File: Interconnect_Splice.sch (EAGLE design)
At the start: 4 parts, among them J1 POWER_JACKPTH, J2 POWER_JACKPTH

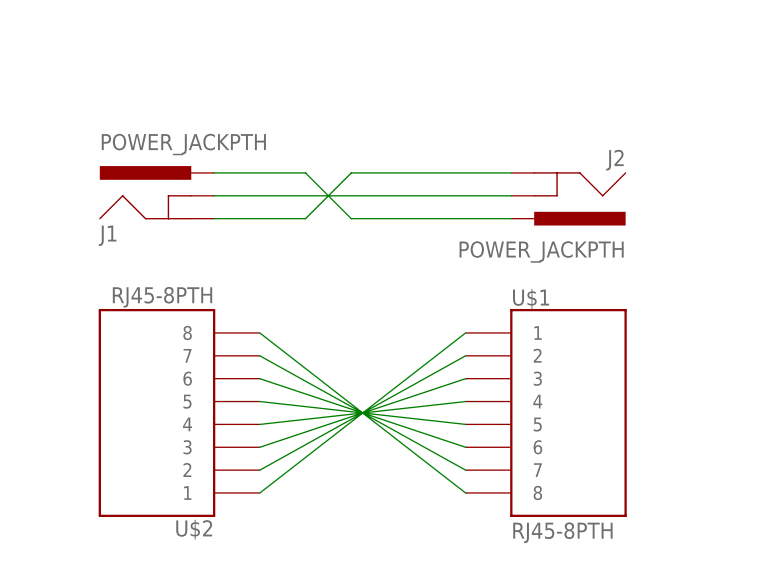
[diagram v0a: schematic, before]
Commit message: fixed bbb cape issue, did something with cable splice
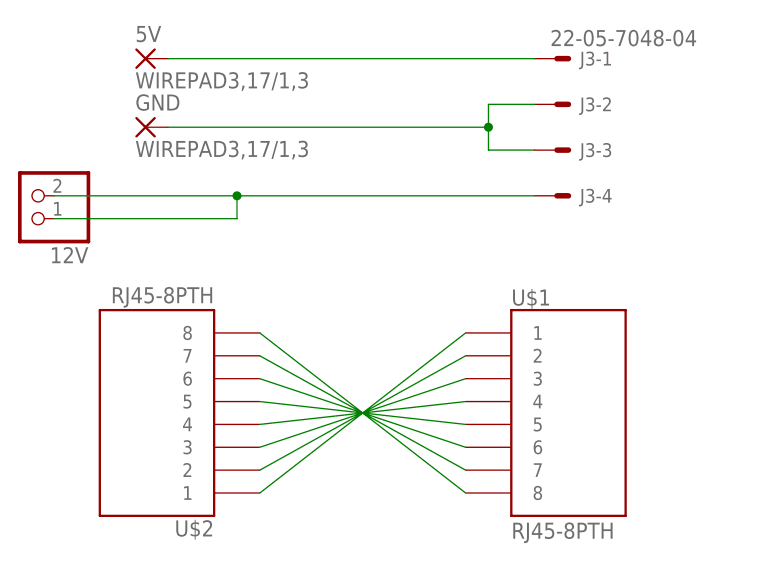
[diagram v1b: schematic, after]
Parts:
- removed J1, J2: POWER_JACKPTH, SparkFun-Connectors:POWER_JACKPTH
- added 12V: (no value), pinhead:PINHD-1X2/90
- added 5V, GND: WIREPAD3,17/1,3, wirepad:WIREPAD3,17/1,3
- added J3: 22-05-7048-04, con-molex:22-05-7048-04
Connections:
- removed net N$1: J1.GND, J2.GND
- new net GND: GND.P, J3-2.S, J3-3.S
- net N$2: now also 5V.P, J3-1.S; no longer J1.GNDBREAK, J2.GNDBREAK
- net N$3: now also 12V.1, 12V.2, J3-4.S; no longer J1.PWR, J2.PWR
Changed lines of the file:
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@@
 <part name="U$1" library="SparkFun-Connectors" deviceset="RJ45-8" device="PTH"/>
 <part name="U$2" library="SparkFun-Connectors" deviceset="RJ45-8" device="PTH"/>
-<part name="J1" library="SparkFun-Connectors" deviceset="POWER_JACK" device="PTH"/>
-<part name="J2" library="SparkFun-Connectors" deviceset="POWER_JACK" device="PTH"/>
+<part name="J3" library="con-molex" deviceset="22-?-04" device="05-7048"/>
+<part name="GND" library="wirepad" deviceset="WIREPAD" device="3,17/1,3" value="WIREPAD3,17/1,3"/>
+<part name="5V" library="wirepad" deviceset="WIREPAD" device="3,17/1,3" value="WIREPAD3,17/1,3"/>
+<part name="12V" library="pinhead" deviceset="PINHD-1X2" device="/90"/>
 </parts>
 <sheets>
@@
 <instance part="U$1" gate="G$1" x="76.2" y="40.64"/>
 <instance part="U$2" gate="G$1" x="27.94" y="43.18" rot="R180"/>
-<instance part="J1" gate="G$1" x="33.02" y="60.96"/>
-<instance part="J2" gate="G$1" x="71.12" y="71.12" rot="R180"/>
+<instance part="J3" gate="-1" x="73.66" y="81.28"/>
+<instance part="J3" gate="-2" x="73.66" y="76.2"/>
+<instance part="J3" gate="-3" x="73.66" y="71.12"/>
+<instance part="J3" gate="-4" x="73.66" y="66.04"/>
+<instance part="GND" gate="G$1" x="27.94" y="73.66"/>
+<instance part="5V" gate="G$1" x="27.94" y="81.28"/>
+<instance part="12V" gate="G$1" x="15.24" y="66.04" rot="R180"/>
 </instances>
 <busses>
 </busses>
 <nets>
-<net name="N$1" class="0">
-<segment>
-<pinref part="J1" gate="G$1" pin="GND"/>
-<wire x1="35.56" y1="63.5" x2="45.72" y2="63.5" width="0.1524" layer="91"/>
-<wire x1="45.72" y1="63.5" x2="50.8" y2="68.58" width="0.1524" layer="91"/>
-<pinref part="J2" gate="G$1" pin="GND"/>
-<wire x1="50.8" y1="68.58" x2="68.58" y2="68.58" width="0.1524" layer="91"/>
-</segment>
-</net>
-<net name="N$2" class="0">
-<segment>
-<pinref part="J2" gate="G$1" pin="GNDBREAK"/>
-<pinref part="J1" gate="G$1" pin="GNDBREAK"/>
-<wire x1="68.58" y1="66.04" x2="35.56" y2="66.04" width="0.1524" layer="91"/>
-</segment>
-</net>
-<net name="N$3" class="0">
-<segment>
-<pinref part="J1" gate="G$1" pin="PWR"/>
-<wire x1="35.56" y1="68.58" x2="45.72" y2="68.58" width="0.1524" layer="91"/>
-<wire x1="45.72" y1="68.58" x2="50.8" y2="63.5" width="0.1524" layer="91"/>
-<pinref part="J2" gate="G$1" pin="PWR"/>
-<wire x1="50.8" y1="63.5" x2="68.58" y2="63.5" width="0.1524" layer="91"/>
-</segment>
-</net>
 <net name="N$4" class="0">
 <segment>
@@
 </segment>
 </net>
+<net name="GND" class="0">
+<segment>
+<pinref part="GND" gate="G$1" pin="P"/>
+<wire x1="30.48" y1="73.66" x2="66.04" y2="73.66" width="0.1524" layer="91"/>
+<wire x1="66.04" y1="73.66" x2="66.04" y2="76.2" width="0.1524" layer="91"/>
+<pinref part="J3" gate="-2" pin="S"/>
+<wire x1="66.04" y1="76.2" x2="71.12" y2="76.2" width="0.1524" layer="91"/>
+<pinref part="J3" gate="-3" pin="S"/>
+<wire x1="71.12" y1="71.12" x2="66.04" y2="71.12" width="0.1524" layer="91"/>
+<wire x1="66.04" y1="71.12" x2="66.04" y2="73.66" width="0.1524" layer="91"/>
+<junction x="66.04" y="73.66"/>
+</segment>
+</net>
+<net name="N$2" class="0">
+<segment>
+<pinref part="J3" gate="-1" pin="S"/>
+<wire x1="71.12" y1="81.28" x2="30.48" y2="81.28" width="0.1524" layer="91"/>
+<pinref part="5V" gate="G$1" pin="P"/>
+</segment>
+</net>
+<net name="N$3" class="0">
+<segment>
+<pinref part="12V" gate="G$1" pin="1"/>
+<wire x1="17.78" y1="63.5" x2="38.1" y2="63.5" width="0.1524" layer="91"/>
+<wire x1="38.1" y1="63.5" x2="38.1" y2="66.04" width="0.1524" layer="91"/>
+<pinref part="12V" gate="G$1" pin="2"/>
+<wire x1="38.1" y1="66.04" x2="17.78" y2="66.04" width="0.1524" layer="91"/>
+<pinref part="J3" gate="-4" pin="S"/>
+<wire x1="71.12" y1="66.04" x2="38.1" y2="66.04" width="0.1524" layer="91"/>
+<junction x="38.1" y="66.04"/>
+</segment>
+</net>
